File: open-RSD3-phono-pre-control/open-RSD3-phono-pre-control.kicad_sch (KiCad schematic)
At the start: 22 parts, among them U1 OPAx134_DIP, U2 OPAx134_DIP

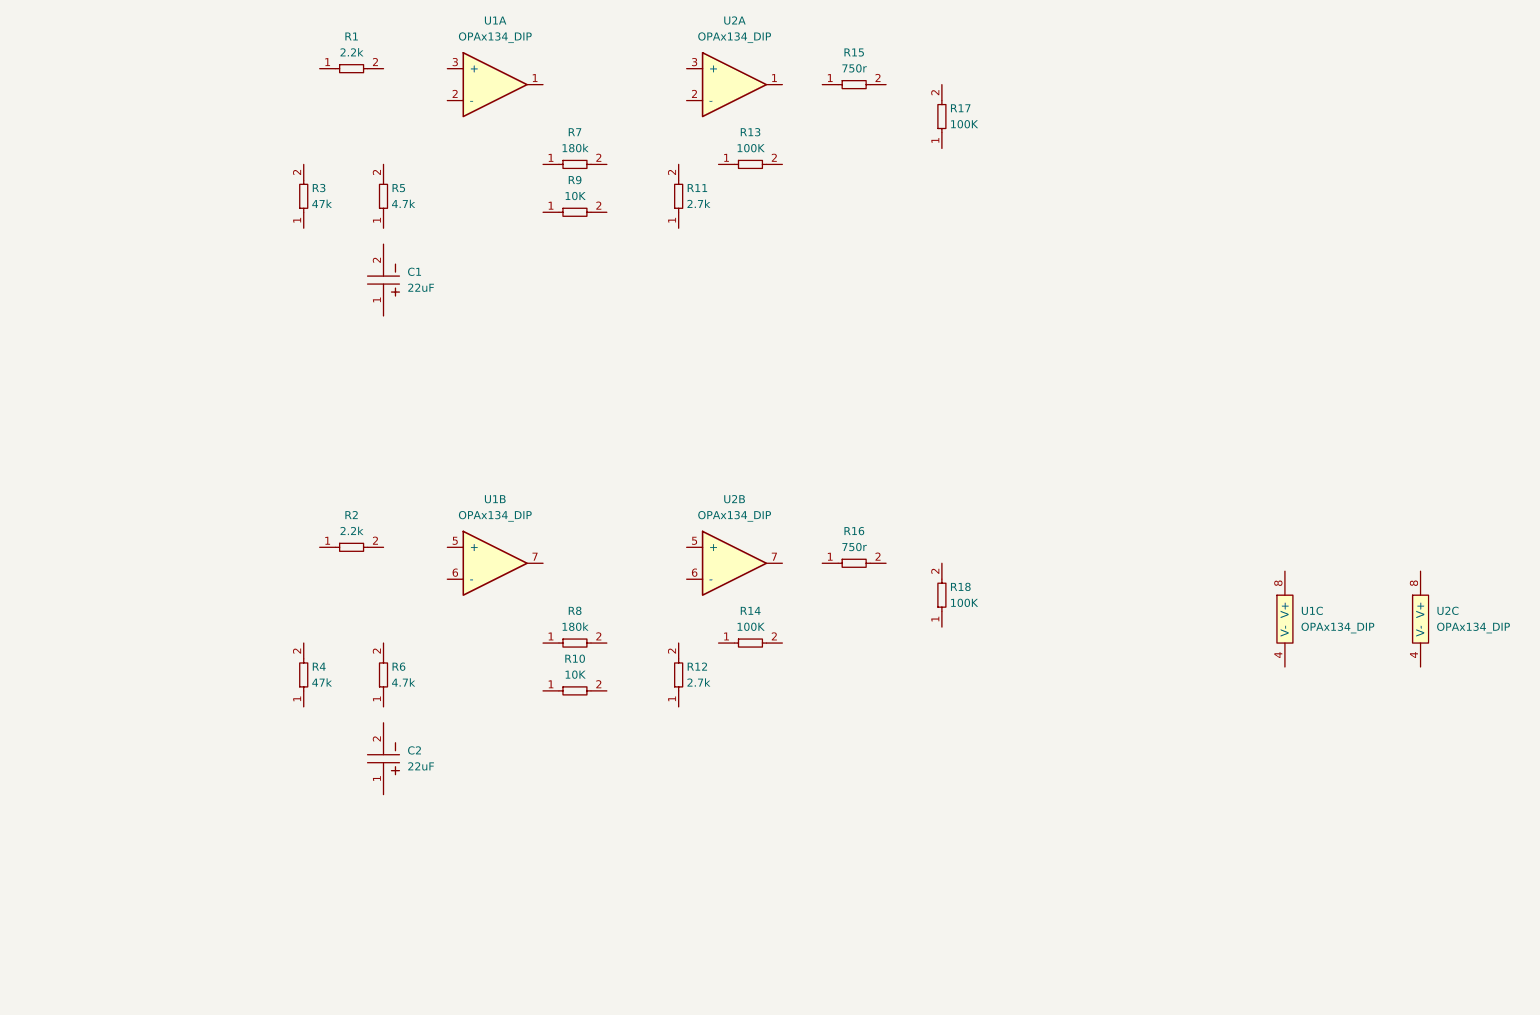
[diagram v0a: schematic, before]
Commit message: Phono Preamp and Power Supply
Phono preamp circuit and power supply added to schematic.
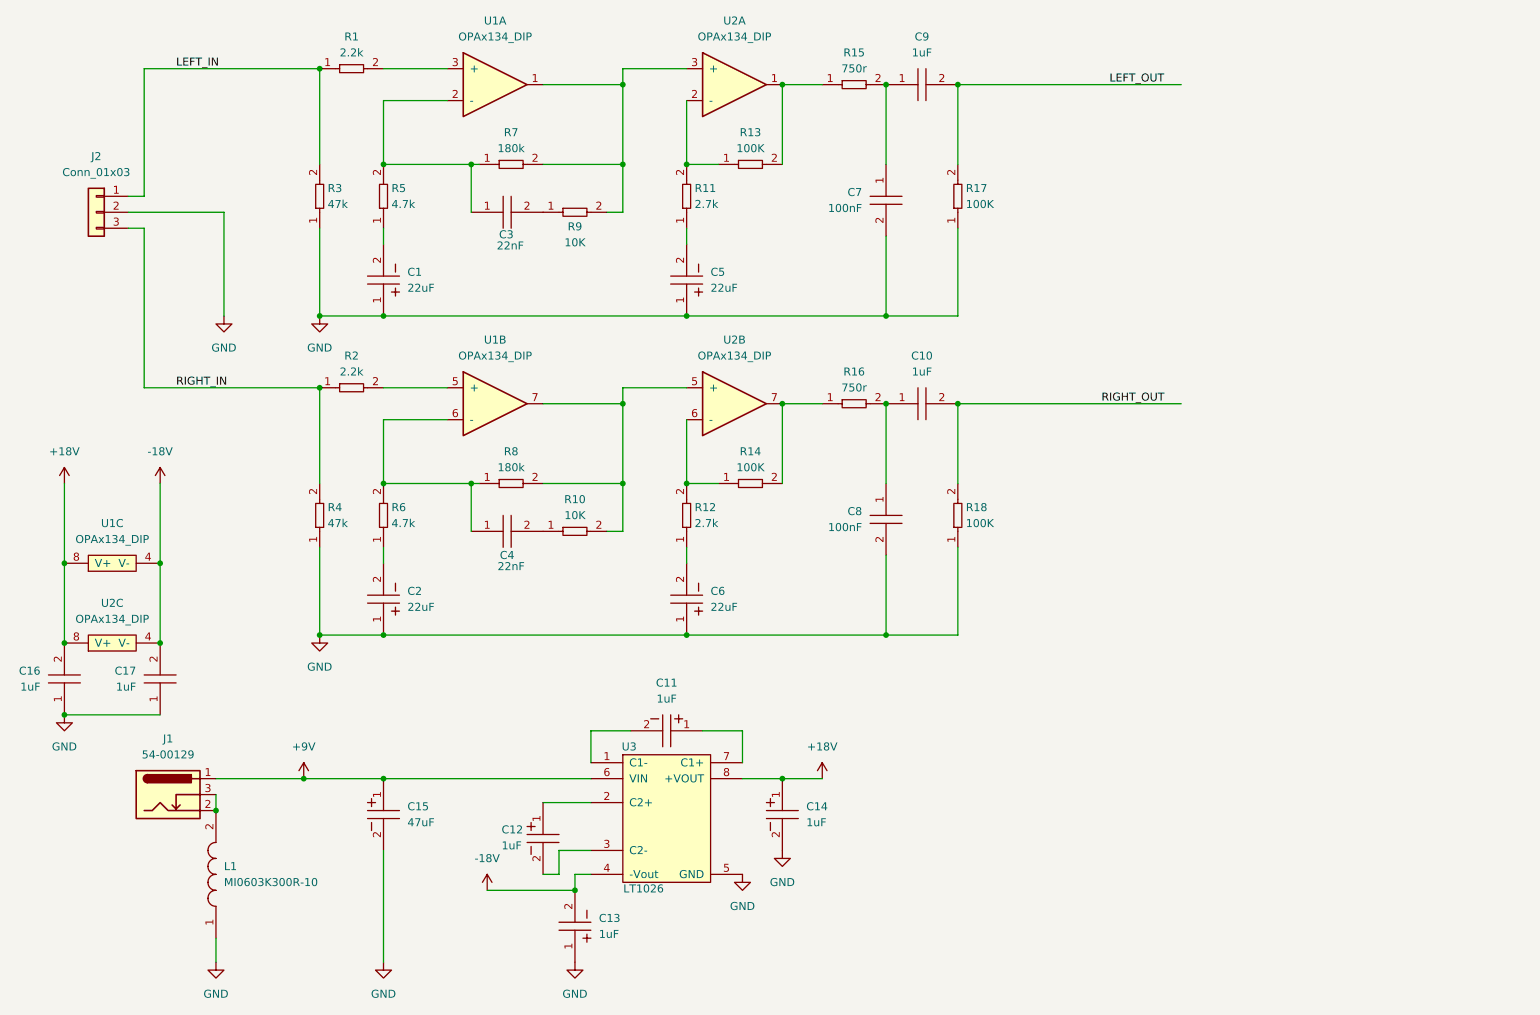
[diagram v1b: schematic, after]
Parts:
- added C10, C9: BFC241671005, AVR-KiCAD-Lib-Capacitors:BFC241671005, symbol AVR-KiCAD-Lib-Capacitors:BFC241671005
- added C11, C12, C13, C14: EEE-1HA010NR, AVR-KiCAD-Lib-Capacitors:EEE-1HA010NR, symbol AVR-KiCAD-Lib-Capacitors:EEE-1HA010NR
- added C15: UUQ1H470MCL1GS, AVR-KiCAD-Lib-Capacitors:CP_Elec_8x10, symbol AVR-KiCAD-Lib-Capacitors:UUQ1H470MCL1GS
- added C16, C17: ECP-U1C105MA5, AVR-KiCAD-Lib-Capacitors:C1210, symbol AVR-KiCAD-Lib-Capacitors:ECP-U1C105MA5
- added C3, C4: MKP1837322161G, AVR-KiCAD-Lib-Capacitors:MKP1837322161G, symbol AVR-KiCAD-Lib-Capacitors:MKP1837322161G
- added C5: UUQ1H220MCL1GS, AVR-KiCAD-Lib-Capacitors:CP_Elec_8x6.5, symbol AVR-KiCAD-Lib-Capacitors:UUQ1H220MCL1GS
- added C6: UUQ1H220MCL1GS, AVR-KiCAD-Lib-Capacitors:CAP_UCD_8X6P2_NCH-M, symbol AVR-KiCAD-Lib-Capacitors:UUQ1H220MCL1GS
- added C7, C8: MKP1837410011, AVR-KiCAD-Lib-Capacitors:MKP1837322161G, symbol AVR-KiCAD-Lib-Capacitors:MKP1837410011
- added J1: 54-00129, AVR-KiCAD-Lib-Connectors:BarrelJack_Horizontal, symbol AVR-KiCAD-Lib-Connectors:54-00129
- added J2: Conn_01x03, symbol Connector_Generic:Conn_01x03
- added L1: MI0603K300R-10, AVR-KiCAD-Lib-Inductors:MI0603K300R-10, symbol AVR-KiCAD-Lib-Inductors:MI0603K300R-10
- added U3: LT1026, AVR-KiCAD-Lib-ICs:DIP8, symbol AVR-KiCAD-Lib-ICs:LT1026
- C2: footprint AVR-KiCAD-Lib-Capacitors:CP_Elec_8x6.5 -> AVR-KiCAD-Lib-Capacitors:CAP_UCD_8X6P2_NCH-M
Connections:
- net at U1.5 (+): now also R2.2
- net at U1.6 (-): now also R6.2, R8.1, C4.1
- net at U1.7: now also R10.2, R8.2, U2.5 (+)
- net GND: now reaches R17.1
- net GND: now also C1.1, C2.1, R18.1, R3.1, R4.1, C13.1, C14.2, C15.2, C16.1, C17.1, C5.1, C6.1, C7.2, C8.2, J2.2 (Pin_2), L1.1, U3.5 (GND)
- net LEFT_OUT: now reaches R17.2
- net LEFT_OUT: now also C9.2
- net at U1.1: now also R7.2, R9.2, U2.3 (+)
- net at U1.2 (-): now also R5.2, R7.1, C3.1
- net at U1.3 (+): now also R1.2
- net LEFT_IN: now reaches R3.2
- net LEFT_IN: now also R1.1, J2.1 (Pin_1)
- net at R12.1: now also C6.2
- net at R12.2: now also R14.1, U2.6 (-)
- net at R11.1: now also C5.2
- net at R11.2: now also R13.1, U2.2 (-)
- net at R6.1: now also C2.2
- net at R14.2: now also R16.1, U2.7
- net at C1.2: now also R5.1
- net RIGHT_OUT: now reaches R18.2
- net RIGHT_OUT: now also C10.2
- net at R13.2: now also R15.1, U2.1
- net at R15.2: now also C7.1, C9.1
- net RIGHT_IN: now reaches R4.2
- net RIGHT_IN: now also R2.1, J2.3 (Pin_3)
- net at R16.2: now also C10.1, C8.1
- net -18V: now reaches U2.4 (V-)
- net -18V: now also U1.4 (V-), C13.2, C17.2, U3.4 (-Vout)
- net +18V: now reaches U2.8 (V+)
- net +18V: now also U1.8 (V+), C14.1, C16.2, U3.8 (+VOUT)
- net at R10.1: now also C4.2
- net at R9.1: now also C3.2
- new net: J1.2, J1.3, L1.2
- new net: C12.1, U3.2 (C2+)
- new net: C12.2, U3.3 (C2-)
- new net: C11.1, U3.7 (C1+)
- new net: C11.2, U3.1 (C1-)
- new net +9V: C15.1, J1.1, U3.6 (VIN)
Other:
- moved on the sheet: C2, R10, R11, R12, R14, R16, R17, R18, R2, R3, R4, R6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

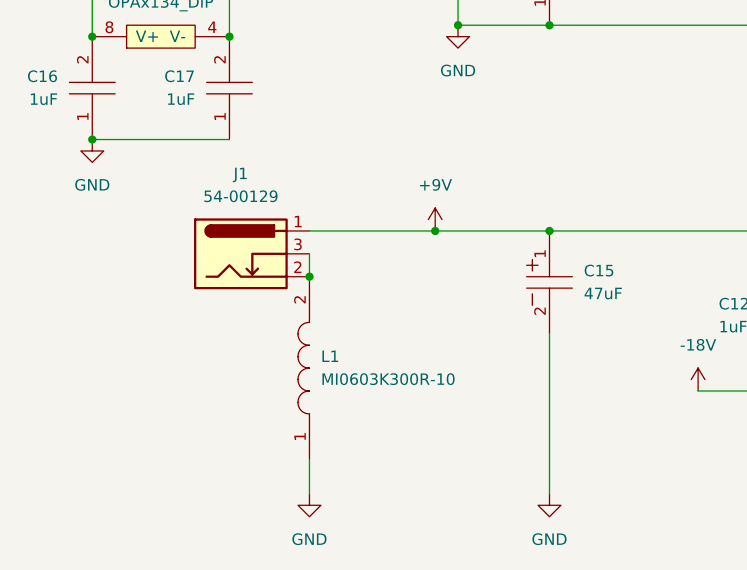
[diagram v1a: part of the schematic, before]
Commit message: Power Project
Created KiCAD project for powersupply and IO Board. This PCB will contain USB-C Power delivery and all input output connectors for the open-RSD3 mini turntable.
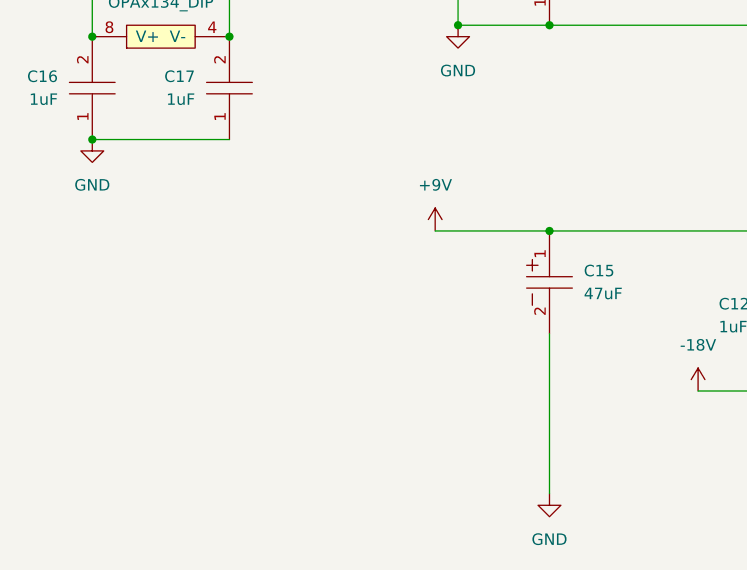
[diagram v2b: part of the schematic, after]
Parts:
- removed J1: 54-00129, AVR-KiCAD-Lib-Connectors:BarrelJack_Horizontal, symbol AVR-KiCAD-Lib-Connectors:54-00129
- removed L1: MI0603K300R-10, AVR-KiCAD-Lib-Inductors:MI0603K300R-10, symbol AVR-KiCAD-Lib-Inductors:MI0603K300R-10
